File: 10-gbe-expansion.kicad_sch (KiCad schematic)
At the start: 0 parts

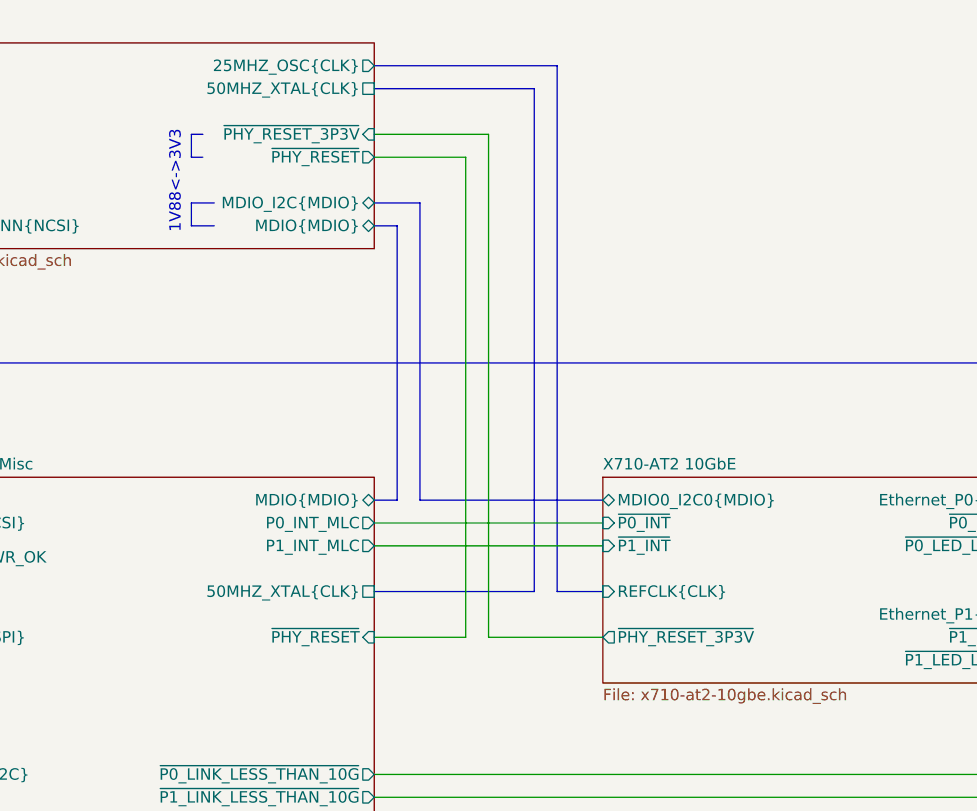
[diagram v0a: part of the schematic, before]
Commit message: [#80813] Change 3V3 and 1V88 power rails names
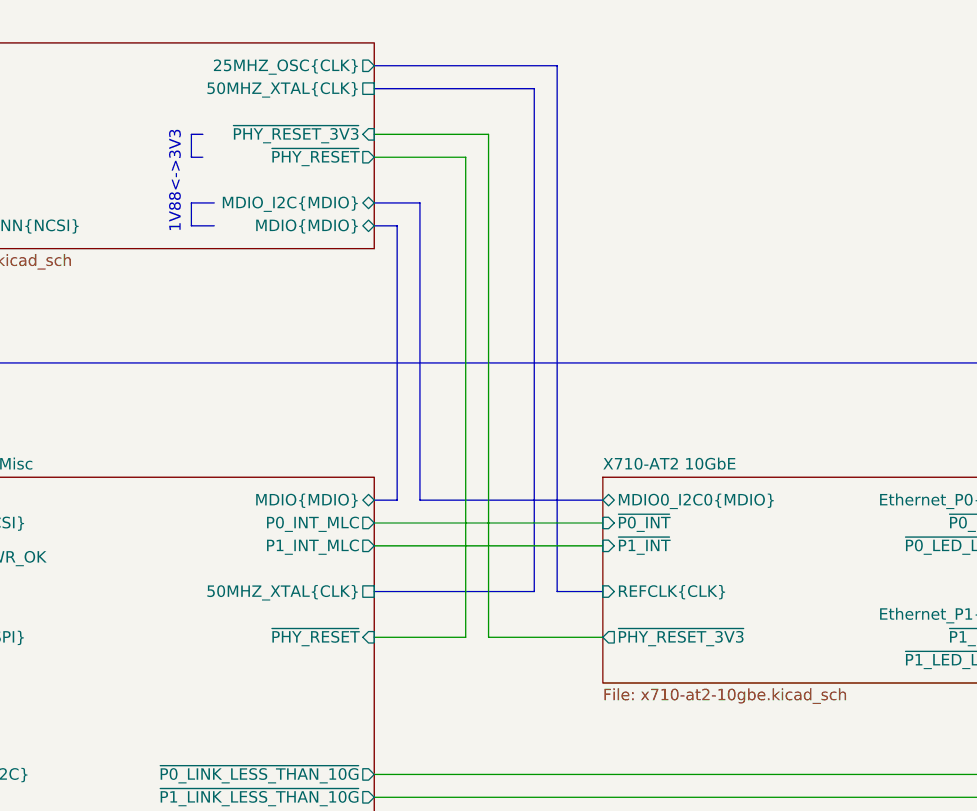
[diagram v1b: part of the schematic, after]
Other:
- sheet Mics ports: added ~{PHY_RESET_3V3}; removed ~{PHY_RESET_3P3V}
- sheet X710-AT2 10GbE ports: added ~{PHY_RESET_3V3}; removed ~{PHY_RESET_3P3V}
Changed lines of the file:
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@@
-			)
-		)
-		(pin "~{PHY_RESET_3P3V}" output
-			(at 228.6 119.38 180)
-			(effects
-				(font
-					(size 1.27 1.27)
-				)
-				(justify left)
 			)
 		)
@@
 		(pin "~{P1_INT}" input
 			(at 228.6 109.22 180)
+			(effects
+				(font
+					(size 1.27 1.27)
+				)
+				(justify left)
+			)
+		)
+		(pin "~{PHY_RESET_3V3}" output
+			(at 228.6 119.38 180)
 			(effects
 				(font
@@
 			)
 		)
-		(pin "~{PHY_RESET_3P3V}" input
-			(at 203.2 63.5 0)
-			(effects
-				(font
-					(size 1.27 1.27)
-				)
-				(justify right)
-			)
-		)
 		(pin "NCSI_CONN{NCSI}" bidirectional
 			(at 152.4 73.66 180)
@@
 			)
 		)
+		(pin "~{PHY_RESET_3V3}" input
+			(at 203.2 63.5 0)
+			(effects
+				(font
+					(size 1.27 1.27)
+				)
+				(justify right)
+			)
+		)

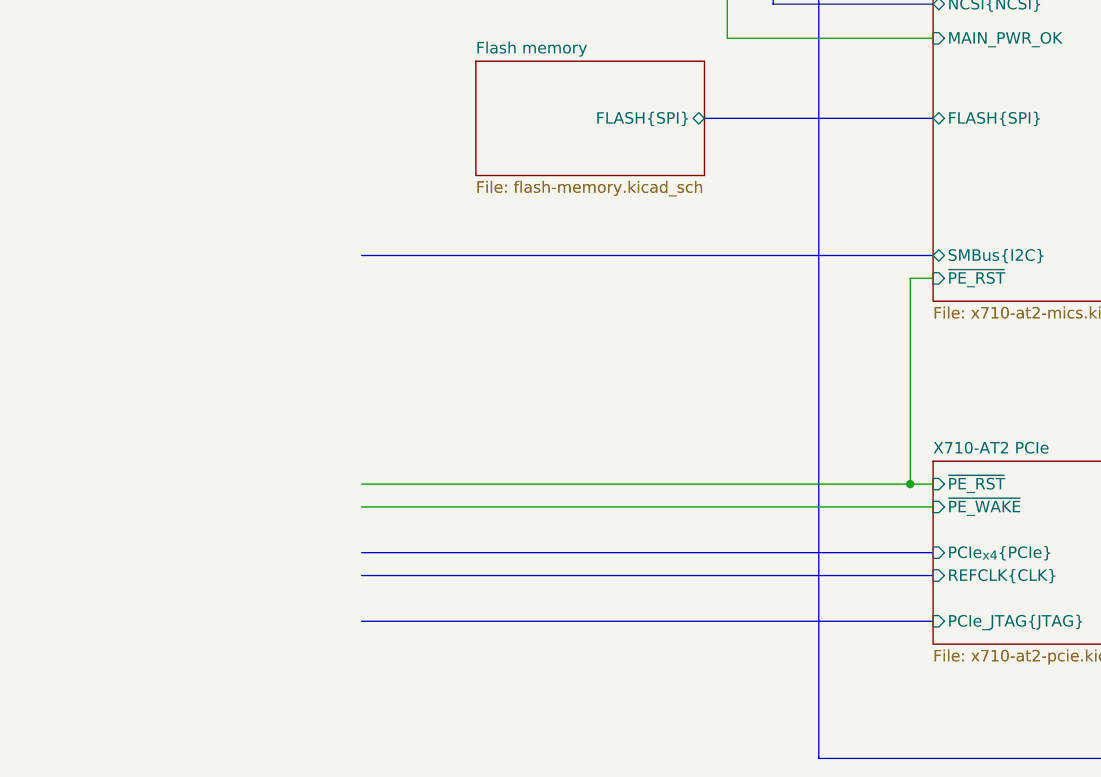
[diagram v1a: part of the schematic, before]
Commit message: [#80813] Add OCuLink connector
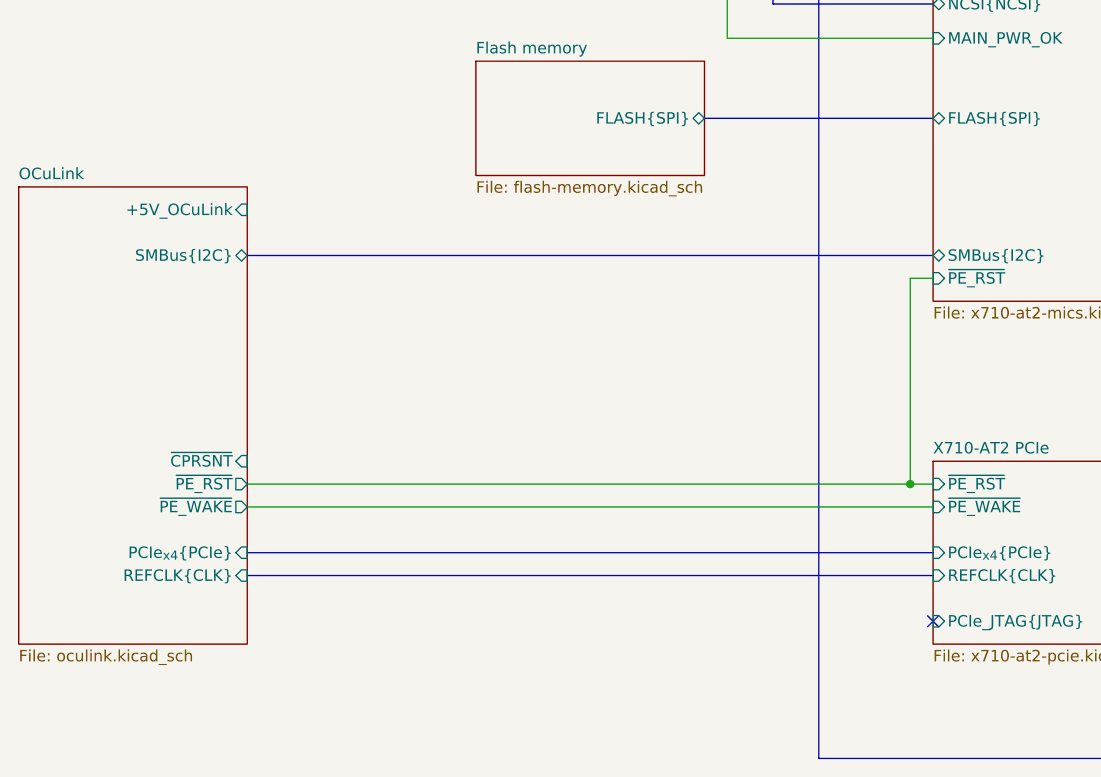
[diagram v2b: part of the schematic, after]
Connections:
- no-connect marks 0 -> 1
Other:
- added sheet OCuLink (oculink.kicad_sch)
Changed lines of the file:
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@@
 		(color 0 0 0 0)
 	)
+	(no_connect
+		(at 152.4 175.26)
+	)
 	(bus
 		(pts
@@
 	(wire
 		(pts
+			(xy 76.2 160.02) (xy 149.86 160.02)
+		)
+		(stroke
+			(width 0)
+			(type default)
+		)
+	)
+	(wire
+		(pts
 			(xy 152.4 137.16) (xy 149.86 137.16)
 		)
@@
 		)
 	)
-	(bus
-		(pts
-			(xy 88.9 167.64) (xy 152.4 167.64)
-		)
-		(stroke
-			(width 0)
-			(type default)
-		)
-	)
 	(wire
 		(pts
@@
 	(bus
 		(pts
+			(xy 76.2 134.62) (xy 152.4 134.62)
+		)
+		(stroke
+			(width 0)
+			(type default)
+		)
+	)
+	(bus
+		(pts
 			(xy 279.4 104.14) (xy 304.8 104.14)
 		)
@@
 	(wire
 		(pts
-			(xy 88.9 162.56) (xy 152.4 162.56)
-		)
-		(stroke
-			(width 0)
-			(type default)
-		)
-	)
-	(wire
-		(pts
 			(xy 129.54 110.49) (xy 129.54 95.25)
 		)
@@
 		)
 	)
+	(wire
+		(pts
+			(xy 76.2 162.56) (xy 152.4 162.56)
+		)
+		(stroke
+			(width 0)
+			(type default)
+		)
+	)
 	(bus
 		(pts
@@
 	(bus
 		(pts
-			(xy 88.9 134.62) (xy 152.4 134.62)
+			(xy 76.2 167.64) (xy 152.4 167.64)
 		)
 		(stroke
@@
 		)
 	)
-	(wire
-		(pts
-			(xy 88.9 160.02) (xy 149.86 160.02)
-		)
-		(stroke
-			(width 0)
-			(type default)
-		)
-	)
 	(bus
 		(pts
@@
 		)
 	)
-	(bus
-		(pts
-			(xy 88.9 170.18) (xy 152.4 170.18)
-		)
-		(stroke
-			(width 0)
-			(type default)
-		)
-	)
 	(polyline
 		(pts
@@
 	(bus
 		(pts
-			(xy 88.9 175.26) (xy 152.4 175.26)
+			(xy 76.2 170.18) (xy 152.4 170.18)
 		)
 		(stroke
@@
 		)
 	)
+	(sheet
+		(at 50.8 127)
+		(size 25.4 50.8)
+		(exclude_from_sim no)
+		(in_bom yes)
+		(on_board yes)
+		(dnp no)
+		(fields_autoplaced yes)
+		(stroke
+			(width 0.1524)
+			(type solid)
+		)
+		(fill
+			(color 255 255 194 1.0000)
+		)
+		(property "Sheetname" "OCuLink"
+			(at 50.8 126.2884 0)
+			(effects
+				(font
+					(size 1.27 1.27)
+				)
+				(justify left bottom)
+			)
+		)
+		(property "Sheetfile" "oculink.kicad_sch"
+			(at 50.8 178.3846 0)
+			(effects
+				(font
+					(size 1.27 1.27)
+				)
+				(justify left top)
+			)
+		)
+		(pin "PCIe_{x4}{PCIe}" input
+			(at 76.2 167.64 0)
+			(effects
+				(font
+					(size 1.27 1.27)
+				)
+				(justify right)
+			)
+		)
+		(pin "REFCLK{CLK}" input
+			(at 76.2 170.18 0)
+			(effects
+				(font
+					(size 1.27 1.27)
+				)
+				(justify right)
+			)
+		)
+		(pin "~{PE_RST}" output
+			(at 76.2 160.02 0)
+			(effects
+				(font
+					(size 1.27 1.27)
+				)
+				(justify right)
+			)
+		)
+		(pin "~{PE_WAKE}" output
+			(at 76.2 162.56 0)
+			(effects
+				(font
+					(size 1.27 1.27)
+				)
+				(justify right)
+			)
+		)
+		(pin "SMBus{I2C}" bidirectional
+			(at 76.2 134.62 0)
+			(effects
+				(font
+					(size 1.27 1.27)
+				)
+				(justify right)
+			)
+		)
+		(pin "+5V_OCuLink" input
+			(at 76.2 129.54 0)
+			(effects
+				(font
+					(size 1.27 1.27)
+				)
+				(justify right)
+			)
+		)
+		(pin "~{CPRSNT}" input
+			(at 76.2 157.48 0)
+			(effects
+				(font
+					(size 1.27 1.27)
+				)
+				(justify right)
+			)
+		)
+		(instances
+			(project "10-gbe-expansion"
+				(path "/04bda987-e5eb-48b4-9e90-d8211dc11b39"
+					(page "11")
+				)
+			)
+		)
+	)

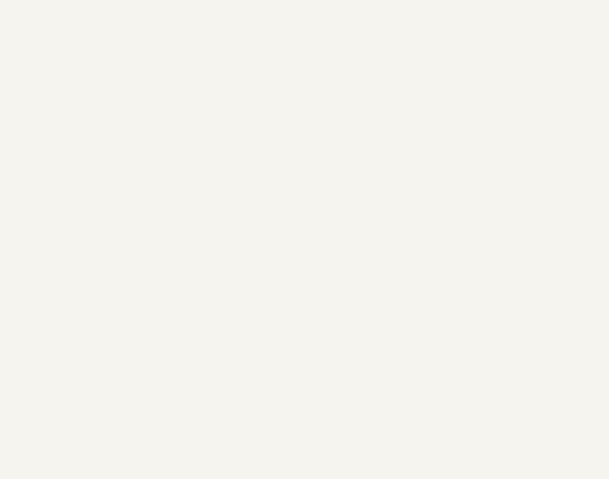
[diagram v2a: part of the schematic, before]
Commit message: [#80813] Add power input connectors, heatsink, mounting, draft component placement
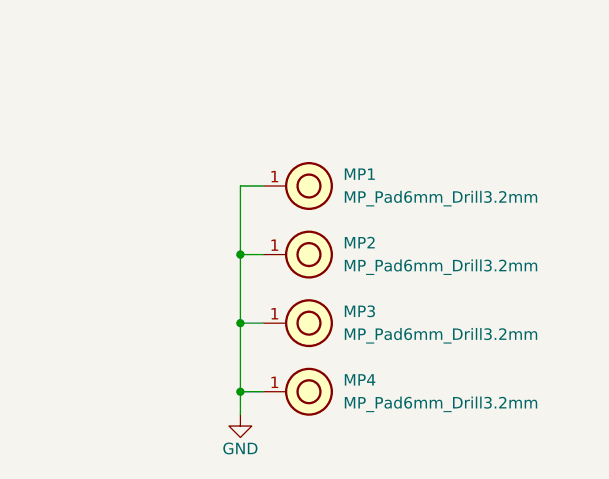
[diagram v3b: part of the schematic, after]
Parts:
- added MP1, MP2, MP3, MP4: MP_Pad6mm_Drill3.2mm, antmicro-footprints:MP_Pad6mm_Drill3.2mm, symbol antmicroMechanicalParts:MP_Pad6mm_Drill3.2mm
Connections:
- new net GND: MP1.1, MP2.1, MP3.1, MP4.1

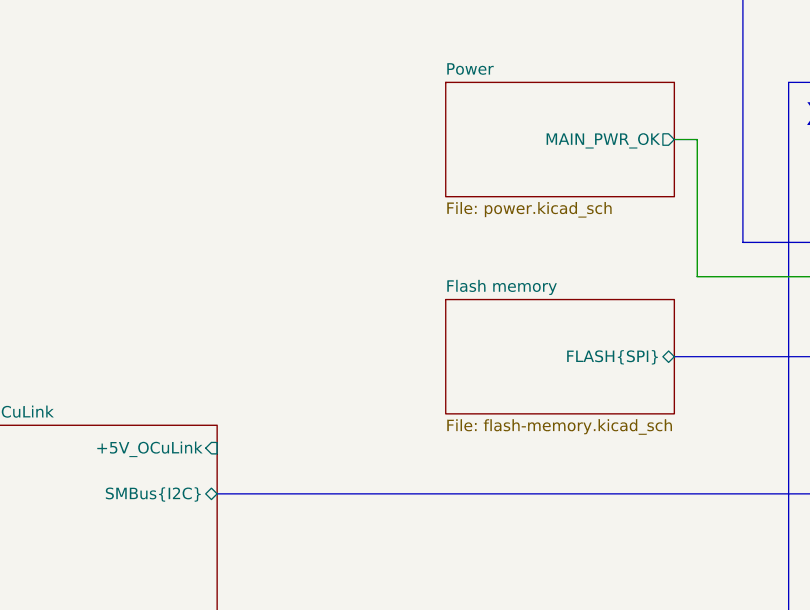
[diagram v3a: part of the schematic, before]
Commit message: [#80813] Add power ORing
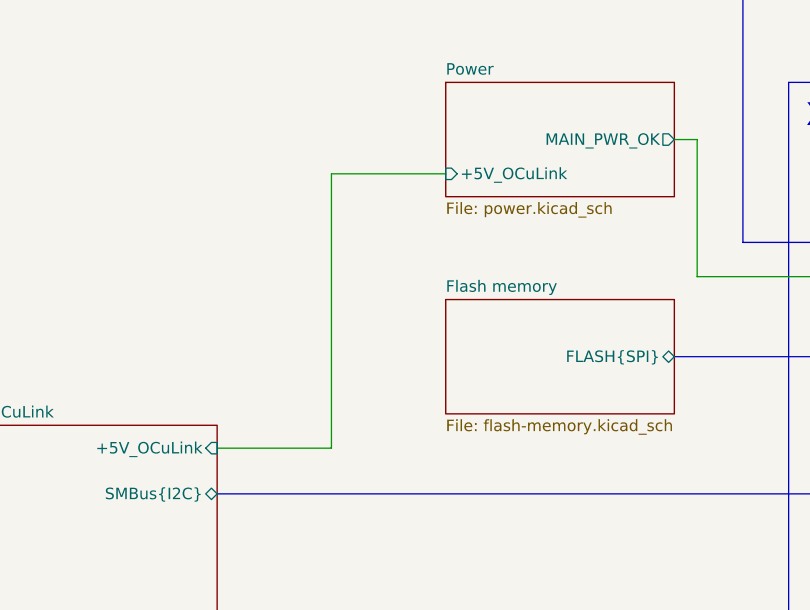
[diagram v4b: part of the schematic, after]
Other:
- sheet Power ports: added +5V_OCuLink; removed none
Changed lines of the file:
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@@
+		)
+	)
+	(wire
+		(pts
+			(xy 88.9 99.06) (xy 88.9 129.54)
+		)
+		(stroke
+			(width 0)
+			(type default)
 		)
 	)
@@
 	(wire
 		(pts
+			(xy 101.6 99.06) (xy 88.9 99.06)
+		)
+		(stroke
+			(width 0)
+			(type default)
+		)
+	)
+	(wire
+		(pts
 			(xy 152.4 110.49) (xy 129.54 110.49)
 		)
@@
 		(pts
 			(xy 279.4 121.92) (xy 304.8 121.92)
+		)
+		(stroke
+			(width 0)
+			(type default)
+		)
+	)
+	(wire
+		(pts
+			(xy 88.9 129.54) (xy 76.2 129.54)
 		)
 		(stroke
@@
 			)
 		)
+		(pin "+5V_OCuLink" input
+			(at 101.6 99.06 180)
+			(effects
+				(font
+					(size 1.27 1.27)
+				)
+				(justify left)
+			)
+		)

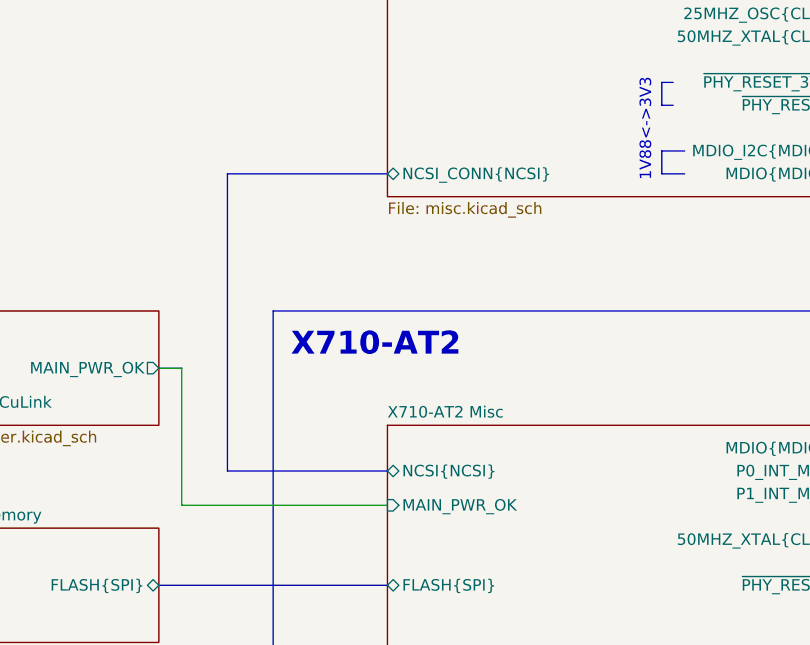
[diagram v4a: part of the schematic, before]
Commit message: [#80813] Change PCB mounts, replace NCSI connector with testpoints
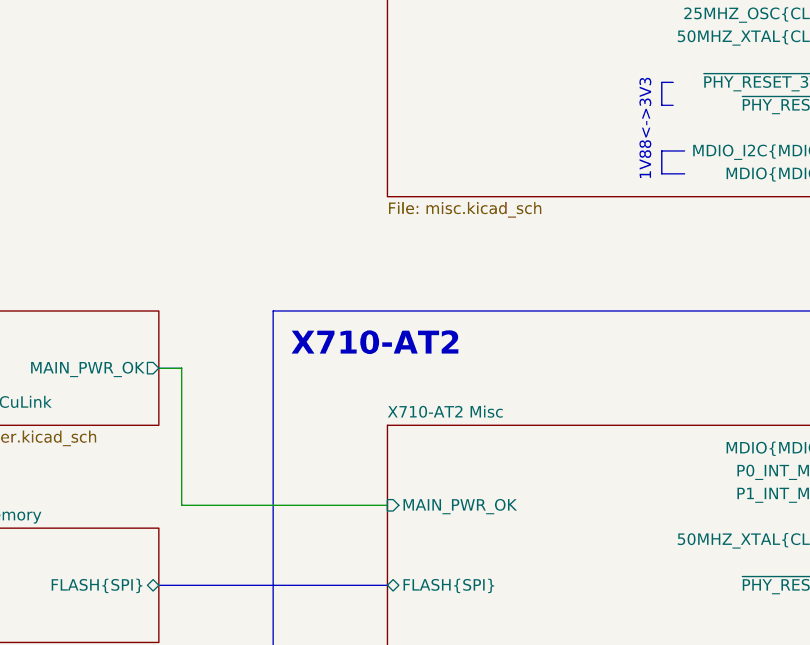
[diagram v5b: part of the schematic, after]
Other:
- sheet Mics ports: added none; removed NCSI_CONN{NCSI}
- sheet X710-AT2 Misc ports: added none; removed NCSI{NCSI}
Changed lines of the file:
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@@
+		)
+	)
+	(wire
+		(pts
+			(xy 326.39 204.47) (xy 323.85 204.47)
+		)
+		(stroke
+			(width 0)
+			(type default)
 		)
 	)
 	(bus
 		(pts
-			(xy 134.62 73.66) (xy 134.62 106.68)
+			(xy 203.2 73.66) (xy 205.74 73.66)
 		)
 		(stroke
@@
 	(wire
 		(pts
-			(xy 326.39 204.47) (xy 323.85 204.47)
+			(xy 149.86 160.02) (xy 152.4 160.02)
 		)
 		(stroke
@@
 	(bus
 		(pts
-			(xy 203.2 73.66) (xy 205.74 73.66)
+			(xy 203.2 71.12) (xy 208.28 71.12)
 		)
 		(stroke
@@
 	(wire
 		(pts
-			(xy 149.86 160.02) (xy 152.4 160.02)
+			(xy 127 95.25) (xy 129.54 95.25)
+		)
+		(stroke
+			(width 0)
+			(type default)
+		)
+	)
+	(polyline
+		(pts
+			(xy 182.88 63.5) (xy 184.15 63.5)
 		)
 		(stroke
@@
 	(bus
 		(pts
-			(xy 203.2 71.12) (xy 208.28 71.12)
+			(xy 208.28 104.14) (xy 228.6 104.14)
 		)
 		(stroke
@@
 	(bus
 		(pts
-			(xy 152.4 106.68) (xy 134.62 106.68)
+			(xy 205.74 104.14) (xy 203.2 104.14)
 		)
 		(stroke
@@
 	(wire
 		(pts
-			(xy 127 95.25) (xy 129.54 95.25)
+			(xy 323.85 181.61) (xy 323.85 189.23)
+		)
+		(stroke
+			(width 0)
+			(type default)
+		)
+	)
+	(wire
+		(pts
+			(xy 213.36 66.04) (xy 213.36 119.38)
 		)
 		(stroke
@@
 	(polyline
 		(pts
-			(xy 182.88 63.5) (xy 184.15 63.5)
+			(xy 182.88 73.66) (xy 185.42 73.66)
+		)
+		(stroke
+			(width 0)
+			(type default)
+		)
+	)
+	(wire
+		(pts
+			(xy 203.2 66.04) (xy 213.36 66.04)
+		)
+		(stroke
+			(width 0)
+			(type default)
+		)
+	)
+	(wire
+		(pts
+			(xy 304.8 111.76) (xy 298.45 111.76)
 		)
 		(stroke
@@
 	(bus
 		(pts
-			(xy 208.28 104.14) (xy 228.6 104.14)
+			(xy 279.4 116.84) (xy 304.8 116.84)
+		)
+		(stroke
+			(width 0)
+			(type default)
+		)
+	)
+	(wire
+		(pts
+			(xy 279.4 121.92) (xy 304.8 121.92)
+		)
+		(stroke
+			(width 0)
+			(type default)
+		)
+	)
+	(wire
+		(pts
+			(xy 88.9 129.54) (xy 76.2 129.54)
+		)
+		(stroke
+			(width 0)
+			(type default)
+		)
+	)
+	(wire
+		(pts
+			(xy 149.86 137.16) (xy 149.86 160.02)
+		)
+		(stroke
+			(width 0)
+			(type default)
+		)
+	)
+	(wire
+		(pts
+			(xy 298.45 111.76) (xy 298.45 134.62)
 		)
 		(stroke
@@
 	(bus
 		(pts
-			(xy 205.74 104.14) (xy 203.2 104.14)
+			(xy 76.2 170.18) (xy 152.4 170.18)
 		)
 		(stroke
@@
 	(wire
 		(pts
-			(xy 323.85 181.61) (xy 323.85 189.23)
-		)
-		(stroke
-			(width 0)
-			(type default)
-		)
-	)
-	(wire
-		(pts
-			(xy 213.36 66.04) (xy 213.36 119.38)
-		)
-		(stroke
-			(width 0)
-			(type default)
-		)
-	)
-	(polyline
-		(pts
-			(xy 182.88 73.66) (xy 185.42 73.66)
-		)
-		(stroke
-			(width 0)
-			(type default)
-		)
-	)
-	(wire
-		(pts
-			(xy 203.2 66.04) (xy 213.36 66.04)
-		)
-		(stroke
-			(width 0)
-			(type default)
-		)
-	)
-	(wire
-		(pts
-			(xy 304.8 111.76) (xy 298.45 111.76)
-		)
-		(stroke
-			(width 0)
-			(type default)
-		)
-	)
-	(bus
-		(pts
-			(xy 279.4 116.84) (xy 304.8 116.84)
-		)
-		(stroke
-			(width 0)
-			(type default)
-		)
-	)
-	(wire
-		(pts
-			(xy 279.4 121.92) (xy 304.8 121.92)
-		)
-		(stroke
-			(width 0)
-			(type default)
-		)
-	)
-	(wire
-		(pts
-			(xy 88.9 129.54) (xy 76.2 129.54)
-		)
-		(stroke
-			(width 0)
-			(type default)
-		)
-	)
-	(wire
-		(pts
-			(xy 149.86 137.16) (xy 149.86 160.02)
-		)
-		(stroke
-			(width 0)
-			(type default)
-		)
-	)
-	(wire
-		(pts
-			(xy 298.45 111.76) (xy 298.45 134.62)
-		)
-		(stroke
-			(width 0)
-			(type default)
-		)
-	)
-	(bus
-		(pts
-			(xy 76.2 170.18) (xy 152.4 170.18)
-		)
-		(stroke
-			(width 0)
-			(type default)
-		)
-	)
-	(wire
-		(pts
 			(xy 323.85 196.85) (xy 326.39 196.85)
-		)
-		(stroke
-			(width 0)
-			(type default)
-		)
-	)
-	(bus
-		(pts
-			(xy 152.4 73.66) (xy 134.62 73.66)
 		)
 		(stroke
@@
 			)
 		)
-		(pin "NCSI{NCSI}" bidirectional
-			(at 152.4 106.68 180)
-			(effects
-				(font
-					(size 1.27 1.27)
-				)
-				(justify left)
-			)
-		)
 		(pin "~{PE_RST}" input
 			(at 152.4 137.16 180)
@@
 			)
 		)
-		(pin "NCSI_CONN{NCSI}" bidirectional
-			(at 152.4 73.66 180)
-			(effects
-				(font
-					(size 1.27 1.27)
-				)
-				(justify left)
-			)
-		)
